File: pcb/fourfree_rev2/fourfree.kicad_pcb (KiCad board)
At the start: 2 copper layers, 268.3 x 79.4 mm, 108 parts, among them U1 ProMicro

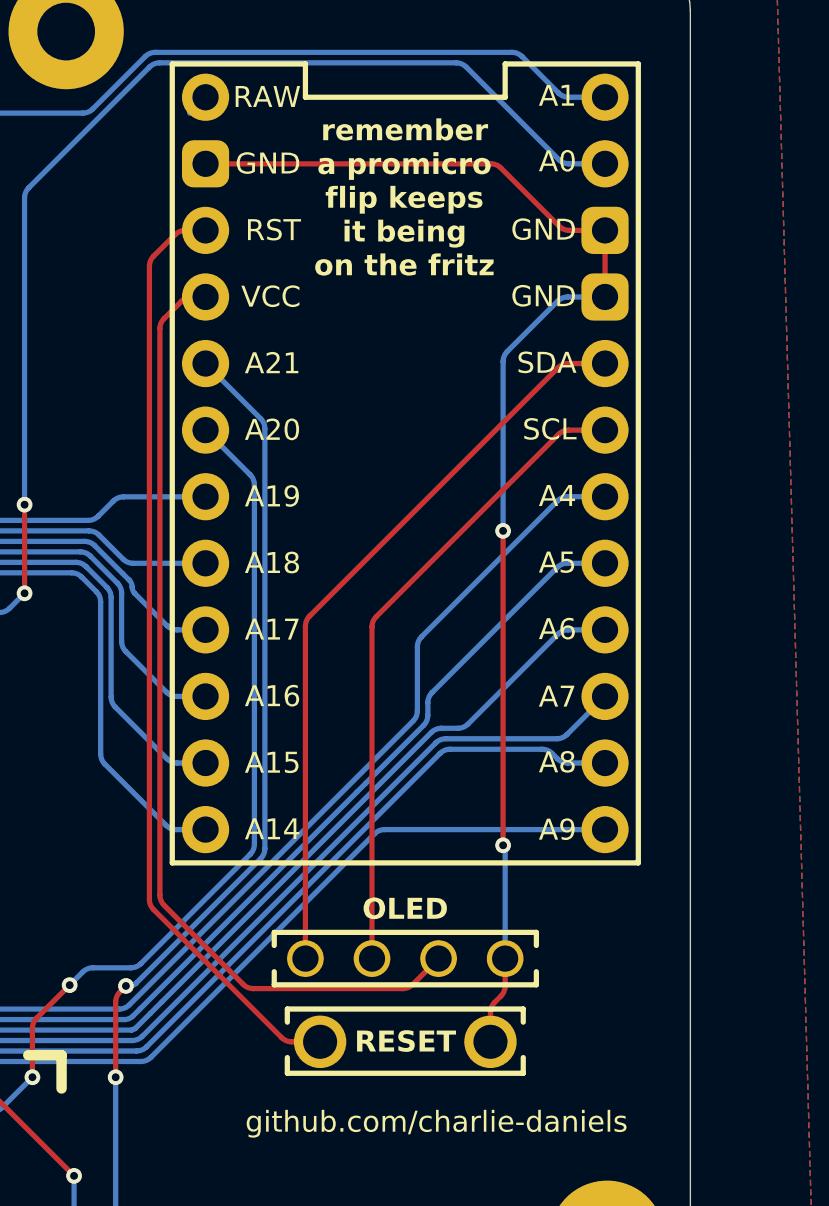
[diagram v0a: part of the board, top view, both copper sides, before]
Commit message: thicken power netclass tracks
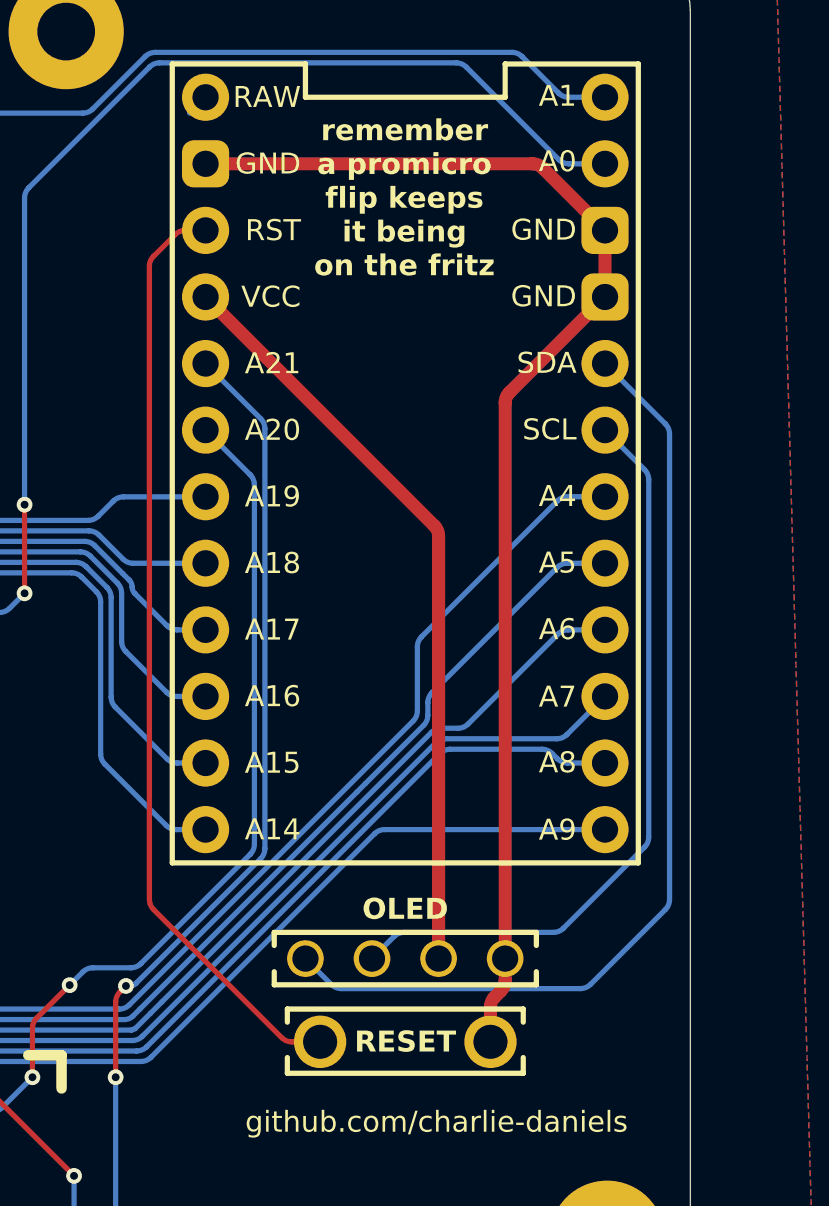
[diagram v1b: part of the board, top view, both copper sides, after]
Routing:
- net SDA: track 28.3 -> 37.3 mm
- net +5V: track 36.6 -> 29.4 mm
- net SCL: track 24.7 -> 28.7 mm
- net GND: track 49.9 -> 49.0 mm, vias 2 -> 0
